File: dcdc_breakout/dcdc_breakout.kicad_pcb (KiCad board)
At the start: 2 copper layers, 14.5 x 33 mm, 12 parts, among them J1 G2116, U1 DC_DC_BREAKOUT

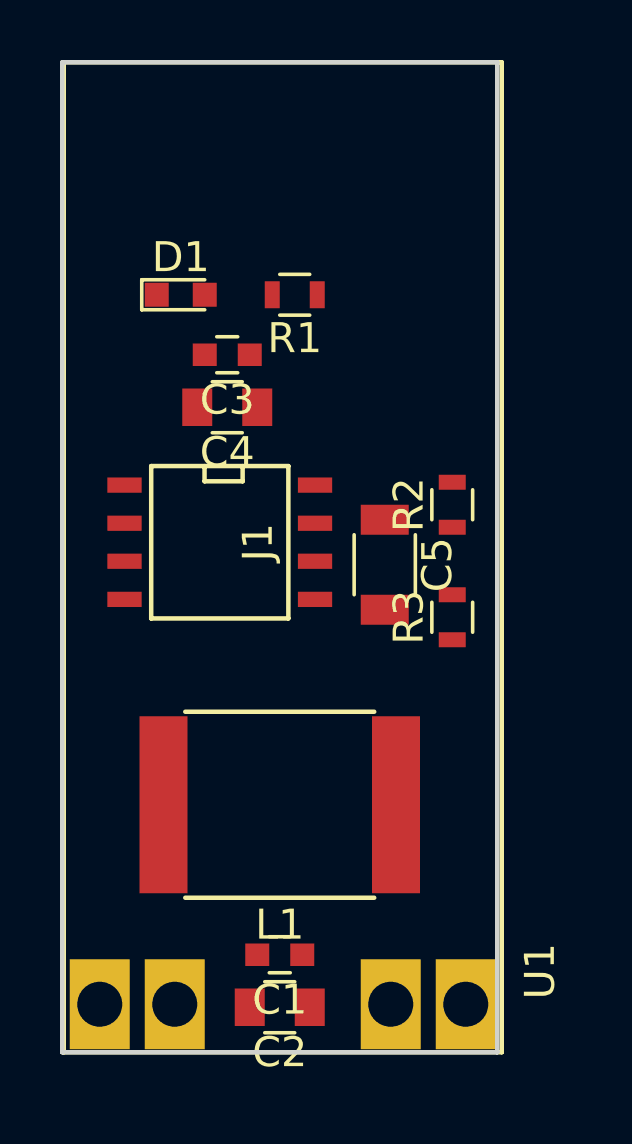
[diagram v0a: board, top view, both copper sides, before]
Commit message: Tweaked the component positioning to match real-life PCB
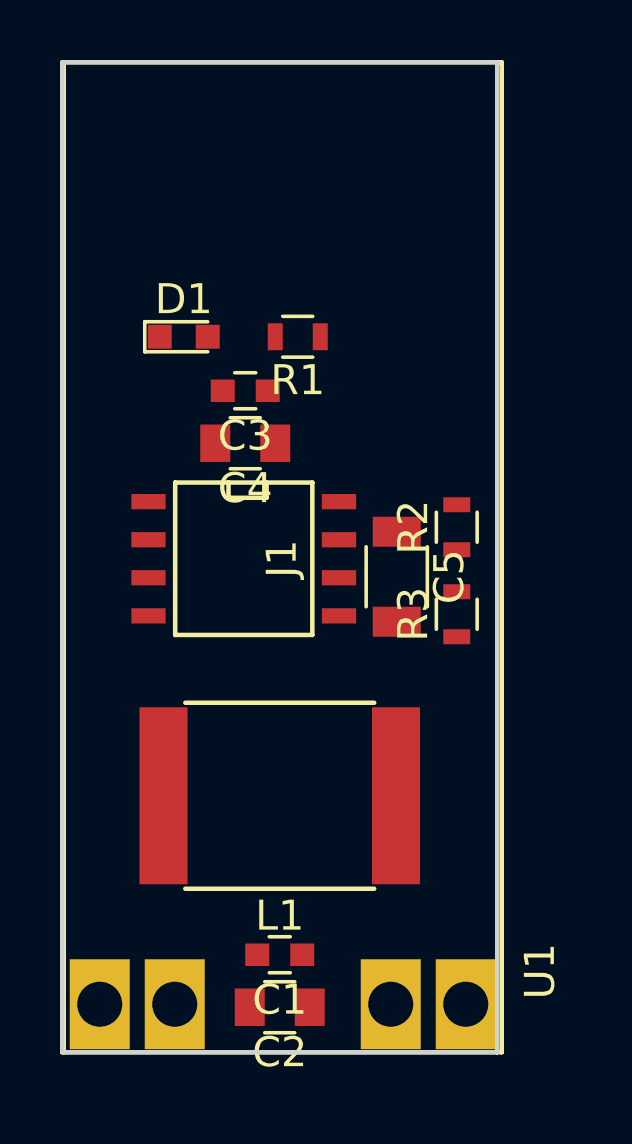
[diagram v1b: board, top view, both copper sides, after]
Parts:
- moved D1 1.40 mm to (145.3, 97.9)
- moved R1 1.40 mm to (149.1, 97.9)
- moved C3 1.34 mm to (147.3, 99.7)
- moved C4 1.34 mm to (147.3, 101.5)
- moved J1 0.97 mm to (147.3, 105.3)
- moved R2 0.76 mm to (154.4, 104.2)
- moved C5 0.57 mm to (152.4, 105.9)
- moved L1 0.30 mm to (148.5, 113.2)
- moved R3 0.18 mm to (154.4, 107.2)
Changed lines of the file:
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@@
   )
   (module Capacitors_SMD:C_0603 (layer F.Cu)
-    (at 146.75 98.5 180)
+    (at 147.35 99.7 180)
     (descr "Capacitor SMD 0603, reflow soldering, AVX (see smccp.pdf)")
     (tags "capacitor 0603")
@@
   )
   (module Capacitors_SMD:C_0805 (layer F.Cu)
-    (at 146.75 100.25 180)
+    (at 147.35 101.45 180)
     (descr "Capacitor SMD 0805, reflow soldering, AVX (see smccp.pdf)")
     (tags "capacitor 0805")
@@
   )
   (module Capacitors_SMD:C_1206 (layer F.Cu)
-    (at 152 105.5 270)
+    (at 152.4 105.9 270)
     (descr "Capacitor SMD 1206, reflow soldering, AVX (see smccp.pdf)")
     (tags "capacitor 1206")
@@
   )
   (module LEDs:LED_0603 (layer F.Cu)
-    (at 145.2 96.5)
+    (at 145.3 97.9)
     (descr "LED 0603 smd package")
     (tags "LED led 0603 SMD smd SMT smt smdled SMDLED smtled SMTLED")
@@
   )
   (module SMD_Packages:SOIC-8-N (layer F.Cu)
-    (at 146.5011 104.75 270)
+    (at 147.3 105.3 270)
     (descr "Module Narrow CMS SOJ 8 pins large")
     (tags "CMS SOJ")
@@
   )
   (module Resistors_SMD:R_0603 (layer F.Cu)
-    (at 149 96.5 180)
+    (at 149.1 97.9 180)
     (descr "Resistor SMD 0603, reflow soldering, Vishay (see dcrcw.pdf)")
     (tags "resistor 0603")
@@
   )
   (module Resistors_SMD:R_0603 (layer F.Cu)
-    (at 154.25 103.5 90)
+    (at 154.4 104.25 90)
     (descr "Resistor SMD 0603, reflow soldering, Vishay (see dcrcw.pdf)")
     (tags "resistor 0603")
@@
   )
   (module Resistors_SMD:R_0603 (layer F.Cu)
-    (at 154.25 107.25 90)
+    (at 154.4 107.15 90)
     (descr "Resistor SMD 0603, reflow soldering, Vishay (see dcrcw.pdf)")
     (tags "resistor 0603")
@@
   )
   (module dcdc_breakout:INDUCTOR (layer F.Cu)
-    (at 148.5 113.5 180)
+    (at 148.5 113.2 180)
     (descr "Inductor, Taiyo Yuden, NR series, Taiyo-Yuden_NR-60xx, 6.0mmx6.0mm")
     (tags "inductor taiyo-yuden nr smd")
